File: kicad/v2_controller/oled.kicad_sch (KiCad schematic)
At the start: 13 parts, among them U2 SSD1306_I2C

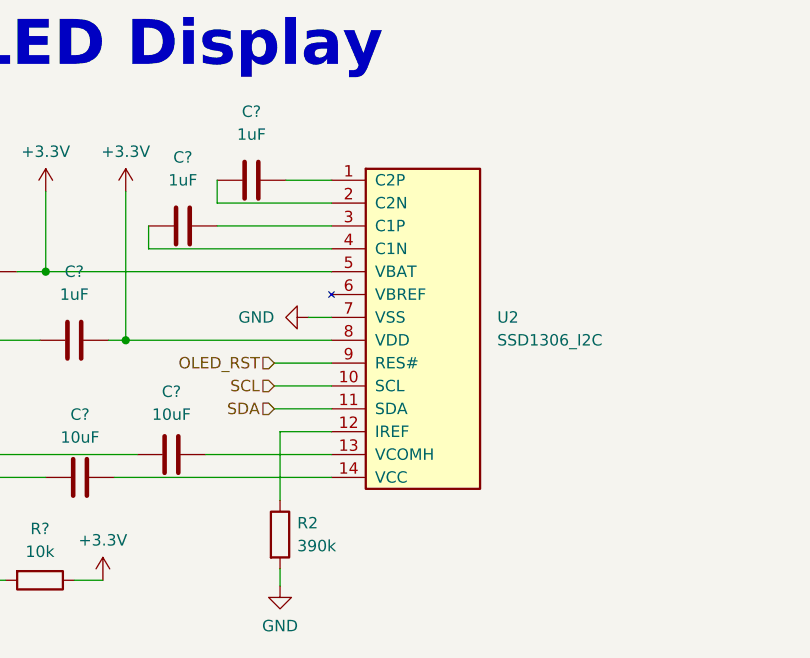
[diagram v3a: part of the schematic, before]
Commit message: [kicad] some additional detail tweaks
- Mark the OLED as not populated (I will manually attach this on the
  bottom of the board).
- Clean up the F.Fab layer
- Add teardrops
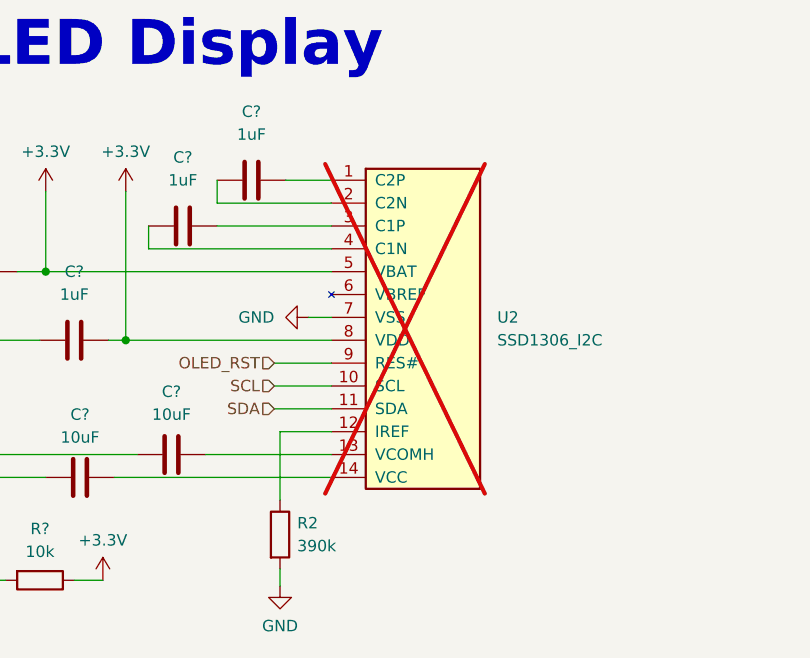
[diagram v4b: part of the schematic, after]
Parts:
- U2: now not fitted; now left out of the parts list
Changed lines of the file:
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@@
   )
   (symbol (lib_id "mantyl:SSD1306_I2C") (at 95.25 56.515 0) (unit 1)
-    (in_bom yes) (on_board yes) (dnp no) (fields_autoplaced)
+    (in_bom no) (on_board yes) (dnp yes) (fields_autoplaced)
     (property "Reference" "U2" (at 103.505 56.515 0)
       (effects (font (size 1.27 1.27)) (justify left))
